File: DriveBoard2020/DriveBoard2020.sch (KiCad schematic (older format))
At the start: 66 parts, among them SW0 SW_SPST, SW1 SW_Push, SW3 SW_Push, SW5 SW_Push, SW7 SW_Push, SW8 SW_Push, SW9 SW_Push, U1 MAX_3232, U2 MAX_3232, U3 OKI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

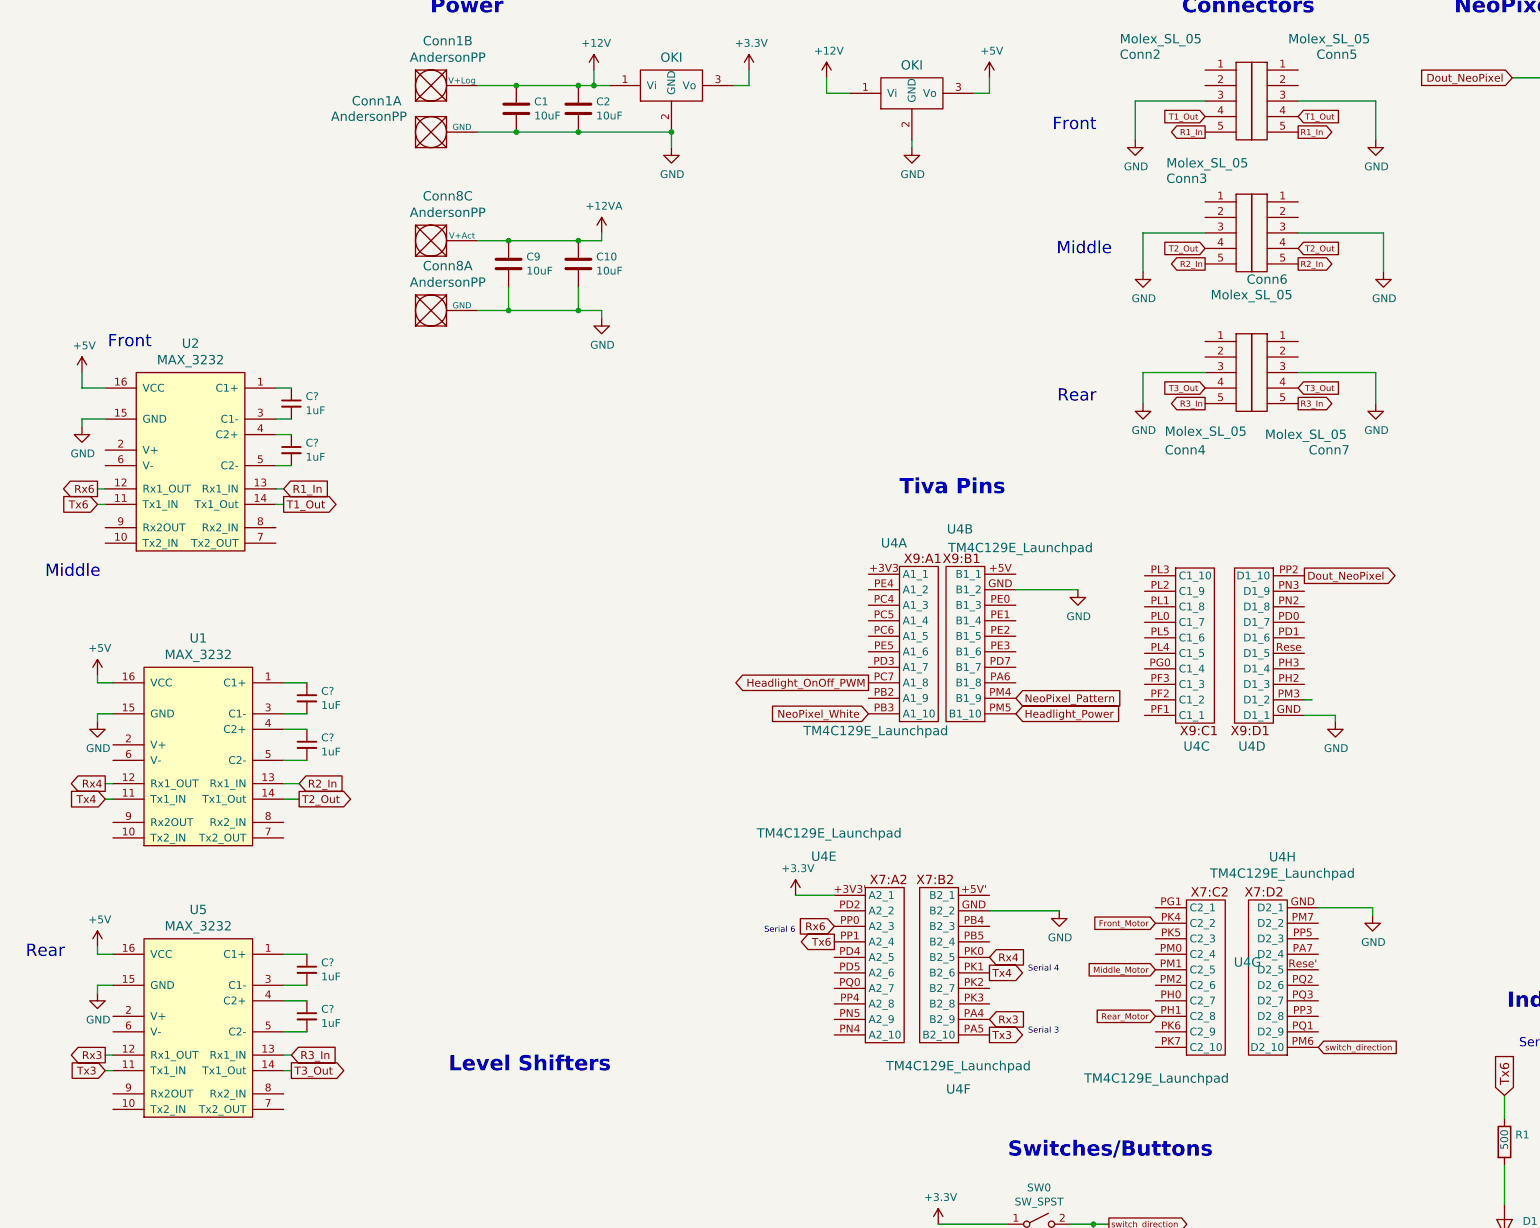
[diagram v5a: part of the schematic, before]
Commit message: added serials and relabled for individual wheel control
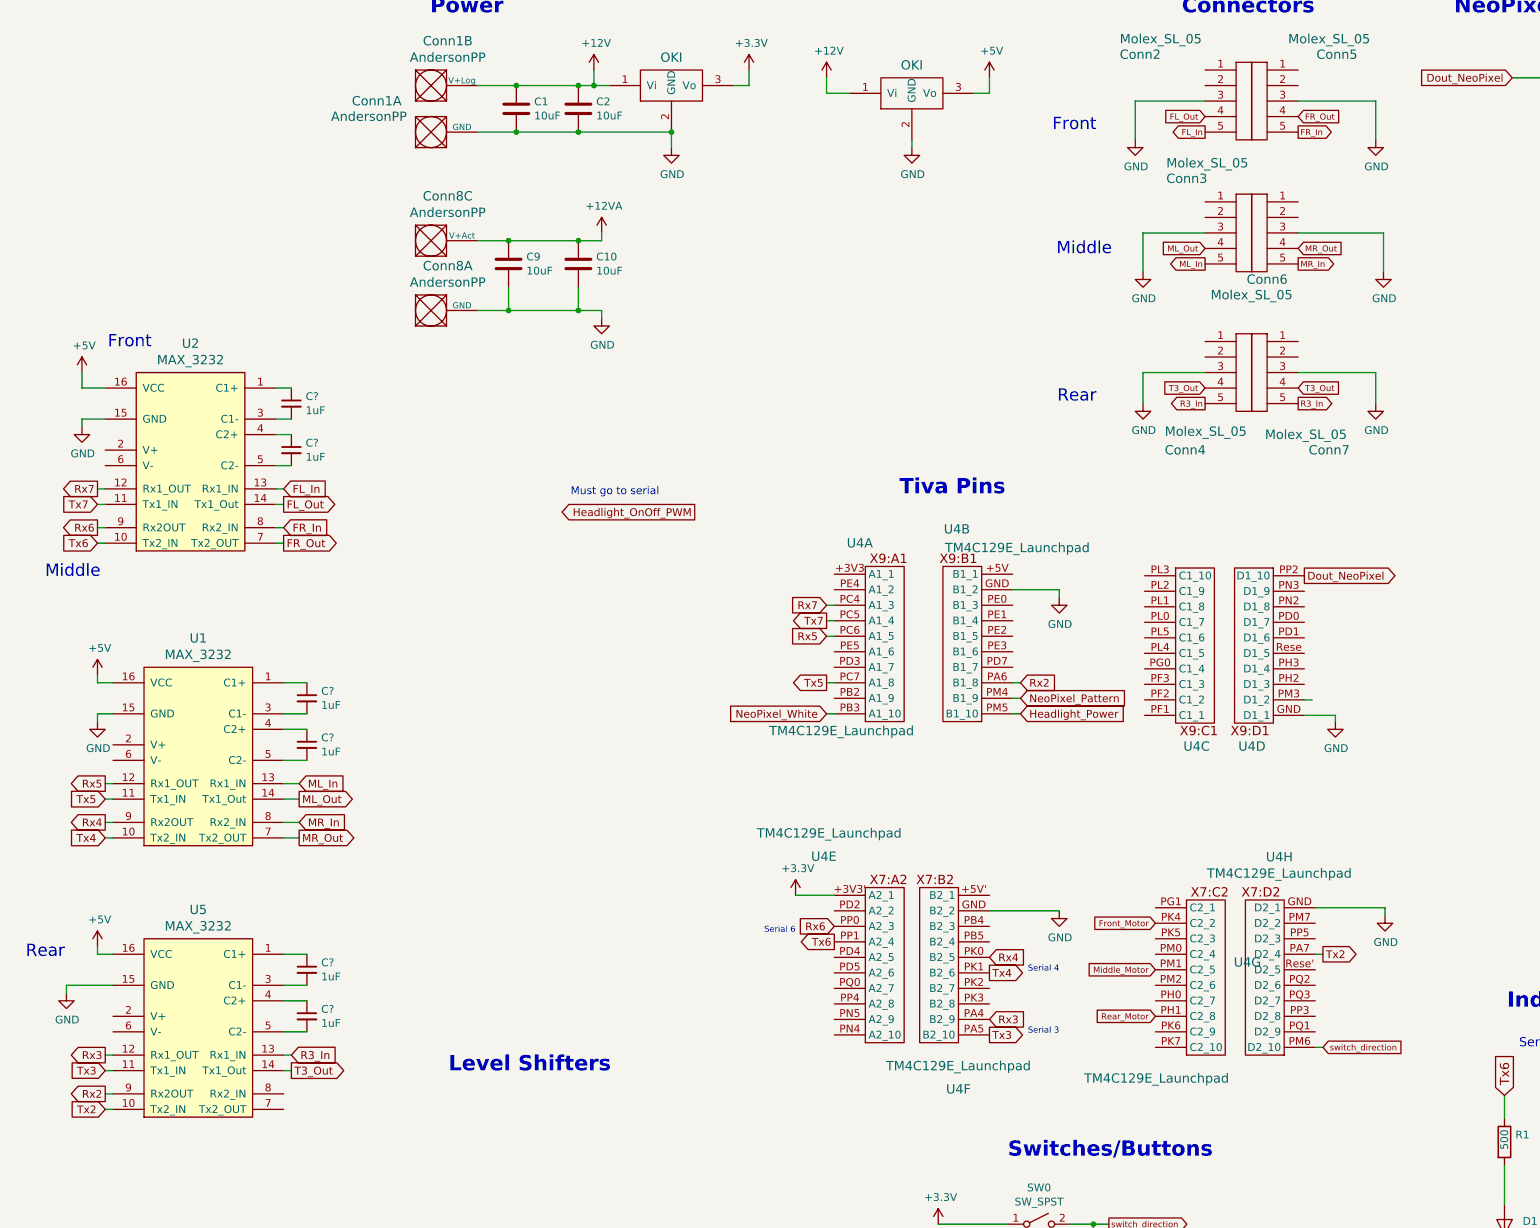
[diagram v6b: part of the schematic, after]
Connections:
- net Headlight_OnOff_PWM: no longer U4.PC7 (A1_8)
- net Rx4: now also U1.9 (Rx2OUT); no longer U1.12 (Rx1_OUT)
- net Rx6: now also U2.9 (Rx2OUT); no longer U2.12 (Rx1_OUT)
- net Tx4: now also U1.10 (Tx2_IN); no longer U1.11 (Tx1_IN)
- net Tx6: now also U2.10 (Tx2_IN); no longer U2.11 (Tx1_IN)
- net FR_Out: now reaches U2.7 (Tx2_OUT)
- net FR_Out: now also Conn5.4
- net FR_In: now reaches U2.8 (Rx2_IN)
- net FR_In: now also Conn5.5
- net Tx2: now reaches U5.10 (Tx2_IN)
- net Tx2: now also U4.PA7 (D2_4)
- net Rx2: now reaches U5.9 (Rx2OUT)
- net Rx2: now also U4.PA6 (B1_8)
- net MR_Out: now reaches U1.7 (Tx2_OUT)
- net MR_Out: now also Conn6.4
- net MR_In: now reaches U1.8 (Rx2_IN)
- net MR_In: now also Conn6.5
- net Rx7: now reaches U4.PC4 (A1_3)
- net Rx7: now also U2.12 (Rx1_OUT)
- net Tx7: now reaches U4.PC5 (A1_4)
- net Tx7: now also U2.11 (Tx1_IN)
- net Rx5: now reaches U4.PC6 (A1_5)
- net Rx5: now also U1.12 (Rx1_OUT)
- net R1_In renamed FL_In
- net FL_In: no longer Conn5.5
- net R2_In renamed ML_In
- net ML_In: no longer Conn6.5
- net T1_Out renamed FL_Out
- net FL_Out: no longer Conn5.4
- net T2_Out renamed ML_Out
- net ML_Out: no longer Conn6.4
- new net Tx5: U1.11 (Tx1_IN), U4.PC7 (A1_8)
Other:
- note added: "Must go to serial"
- moved on the sheet: U4A, U4B, U4H
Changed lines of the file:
@@
 Text GLabel 15300 2340 2    50   Output ~ 0
 NeoPixel_Pattern
-Text GLabel 9270 5250 2    50   Input ~ 0
+Text GLabel 9300 5250 2    50   Input ~ 0
 Headlight_Power
 Wire Wire Line
 	11180 5160 11130 5160
-Text GLabel 8320 5250 0    50   Input ~ 0
-NeoPixel_White
-Text GLabel 9270 5150 2    50   Input ~ 0
+Text GLabel 9300 5150 2    50   Input ~ 0
 NeoPixel_Pattern
 $Comp
@@
 	15020 4050 15020 4100
 Text GLabel 11090 1400 2    39   Input ~ 0
-T1_Out
+FR_Out
 $Comp
 L DriveBoard2020-rescue:Molex_SL_05-MRDT_Connectors-DriveBoard2020-rescue Conn5
@@
 $EndComp
 Text GLabel 11090 1500 2    39   Output ~ 0
-R1_In
+FR_In
 Wire Wire Line
 	3250 3350 3250 3400
@@
 Text GLabel 10170 6600 0    39   Input ~ 0
 Front_Motor
-Text GLabel 11220 7400 2    39   Input ~ 0
+Text GLabel 11250 7400 2    39   Input ~ 0
 switch_direction
 $Comp
@@
 $EndComp
 Text GLabel 10490 1400 0    39   Input ~ 0
-T1_Out
+FL_Out
 Text GLabel 10490 1500 0    39   Output ~ 0
-R1_In
+FL_In
 Text GLabel 10490 3150 0    39   Input ~ 0
 T3_Out
@@
 $EndComp
 Text GLabel 10490 2350 0    39   Output ~ 0
-R2_In
+ML_In
 Text GLabel 10490 2250 0    39   Input ~ 0
-T2_Out
+ML_Out
 $Comp
 L power:GND #PWR0114
@@
 Rear
 Text GLabel 11090 2250 2    39   Input ~ 0
-T2_Out
+MR_Out
 Text GLabel 11090 2350 2    39   Output ~ 0
-R2_In
+MR_In
 Text GLabel 11090 3150 2    39   Input ~ 0
 T3_Out
@@
 Text GLabel 3400 7550 0    50   Input ~ 0
 Tx3
-Text GLabel 4650 5700 2    50   Input ~ 0
-R2_In
-Text GLabel 4650 5800 2    50   Output ~ 0
-T2_Out
-Text GLabel 4550 3800 2    51   Input ~ 0
-R1_In
-Text GLabel 4550 3900 2    51   Output ~ 0
-T1_Out
-Text GLabel 3400 5700 0    50   Output ~ 0
+Text GLabel 4650 5950 2    50   Input ~ 0
+MR_In
+Text GLabel 4650 6050 2    50   Output ~ 0
+MR_Out
+Text GLabel 4550 4050 2    51   Input ~ 0
+FR_In
+Text GLabel 4550 4150 2    51   Output ~ 0
+FR_Out
+Text GLabel 3400 5950 0    50   Output ~ 0
 Rx4
-Text GLabel 3400 5800 0    51   Input ~ 0
+Text GLabel 3400 6050 0    51   Input ~ 0
 Tx4
-Text GLabel 3350 3800 0    50   Output ~ 0
+Text GLabel 3350 4050 0    50   Output ~ 0
 Rx6
-Text GLabel 3350 3900 0    51   Input ~ 0
+Text GLabel 3350 4150 0    51   Input ~ 0
 Tx6
 $Comp
@@
 $Comp
 L MRDT_Shields:TM4C129E_Launchpad U4
-U 1 1 5DE8D46B
-P 8520 5300
-F 0 "U4" H 8400 6450 60  0000 L CNN
-F 1 "TM4C129E_Launchpad" H 7900 5240 60  0000 L CNN
-F 2 "MRDT_Shields:TM4C129E_Launchpad_FULL_THT_BOTTOM" H 8520 5300 60  0001 C CNN
-F 3 "" H 8520 5300 60  0001 C CNN
-	1    8520 5300
-	1    0    0    -1
-$EndComp
-$Comp
-L MRDT_Shields:TM4C129E_Launchpad U4
 U 2 1 5DE90FB1
-P 9070 5300
-F 0 "U4" H 9230 6540 60  0000 C CNN
-F 1 "TM4C129E_Launchpad" H 8840 6420 60  0000 C CNN
-F 2 "MRDT_Shields:TM4C129E_Launchpad_FULL_THT_BOTTOM" H 9070 5300 60  0001 C CNN
-F 3 "" H 9070 5300 60  0001 C CNN
-	2    9070 5300
+P 9050 5300
+F 0 "U4" H 9210 6540 60  0000 C CNN
+F 1 "TM4C129E_Launchpad" H 8820 6420 60  0000 C CNN
+F 2 "MRDT_Shields:TM4C129E_Launchpad_FULL_THT_BOTTOM" H 9050 5300 60  0001 C CNN
+F 3 "" H 9050 5300 60  0001 C CNN
+	2    9050 5300
 	-1   0    0    -1
 $EndComp
@@
 L MRDT_Shields:TM4C129E_Launchpad U4
 U 8 1 5DEDFAF8
-P 11020 7450
-F 0 "U4" H 11051 8727 60  0000 C CNN
-F 1 "TM4C129E_Launchpad" H 11051 8621 60  0000 C CNN
-F 2 "MRDT_Shields:TM4C129E_Launchpad_FULL_THT_BOTTOM" H 11020 7450 60  0001 C CNN
-F 3 "" H 11020 7450 60  0001 C CNN
-	8    11020 7450
+P 11000 7450
+F 0 "U4" H 11031 8727 60  0000 C CNN
+F 1 "TM4C129E_Launchpad" H 11031 8621 60  0000 C CNN
+F 2 "MRDT_Shields:TM4C129E_Launchpad_FULL_THT_BOTTOM" H 11000 7450 60  0001 C CNN
+F 3 "" H 11000 7450 60  0001 C CNN
+	8    11000 7450
 	-1   0    0    -1
 $EndComp
-Text GLabel 8320 5050 0    50   Output ~ 0
-Headlight_OnOff_PWM
 Wire Wire Line
 	11330 5260 11330 5300
@@
 L power:GND #PWR0146
 U 1 1 5E44A8A8
-P 9670 4450
-F 0 "#PWR0146" H 9670 4200 50  0001 C CNN
-F 1 "GND" H 9675 4277 50  0000 C CNN
-F 2 "" H 9670 4450 50  0001 C CNN
-F 3 "" H 9670 4450 50  0001 C CNN
-	1    9670 4450
+P 9550 4500
+F 0 "#PWR0146" H 9550 4250 50  0001 C CNN
+F 1 "GND" H 9555 4327 50  0000 C CNN
+F 2 "" H 9550 4500 50  0001 C CNN
+F 3 "" H 9550 4500 50  0001 C CNN
+	1    9550 4500
 	1    0    0    -1
 $EndComp
@@
 L power:GND #PWR0150
 U 1 1 5E4D6DF7
-P 11570 6550
-F 0 "#PWR0150" H 11570 6300 50  0001 C CNN
-F 1 "GND" H 11575 6377 50  0000 C CNN
-F 2 "" H 11570 6550 50  0001 C CNN
-F 3 "" H 11570 6550 50  0001 C CNN
-	1    11570 6550
+P 11650 6550
+F 0 "#PWR0150" H 11650 6300 50  0001 C CNN
+F 1 "GND" H 11655 6377 50  0000 C CNN
+F 2 "" H 11650 6550 50  0001 C CNN
+F 3 "" H 11650 6550 50  0001 C CNN
+	1    11650 6550
 	1    0    0    -1
 $EndComp
@@
 	1    0    0    -1
 $EndComp
-Wire Wire Line
-	9270 4450 9670 4450
 $Comp
 L power:+5V #PWR0154
@@
 	1    0    0    -1
 $EndComp
-Wire Wire Line
-	11220 6500 11570 6500
-Wire Wire Line
-	11570 6500 11570 6550
 Wire Notes Line
 	11790 9960 11810 9960
@@
 L power:GND #PWR?
 U 1 1 5E239C6D
-P 3350 7050
-F 0 "#PWR?" H 3350 6800 50  0001 C CNN
-F 1 "GND" H 3355 6877 50  0000 C CNN
-F 2 "" H 3350 7050 50  0001 C CNN
-F 3 "" H 3350 7050 50  0001 C CNN
-	1    3350 7050
-	1    0    0    -1
-$EndComp
-Wire Wire Line
-	3450 7000 3350 7000
-Wire Wire Line
-	3350 7000 3350 7050
+P 3150 7050
+F 0 "#PWR?" H 3150 6800 50  0001 C CNN
+F 1 "GND" H 3155 6877 50  0000 C CNN
+F 2 "" H 3150 7050 50  0001 C CNN
+F 3 "" H 3150 7050 50  0001 C CNN
+	1    3150 7050
+	1    0    0    -1
+$EndComp
 $Comp
 L Device:C_Small C?
@@
 	1    0    0    -1
 $EndComp
+$Comp
+L MRDT_Shields:TM4C129E_Launchpad U4
+U 1 1 5DE8D46B
+P 8300 5300
+F 0 "U4" H 8180 6450 60  0000 L CNN
+F 1 "TM4C129E_Launchpad" H 7680 5240 60  0000 L CNN
+F 2 "MRDT_Shields:TM4C129E_Launchpad_FULL_THT_BOTTOM" H 8300 5300 60  0001 C CNN
+F 3 "" H 8300 5300 60  0001 C CNN
+	1    8300 5300
+	1    0    0    -1
+$EndComp
+Text GLabel 8050 5250 0    50   Input ~ 0
+NeoPixel_White
+Text GLabel 7200 3950 0    50   Output ~ 0
+Headlight_OnOff_PWM
+Wire Wire Line
+	8050 5050 8100 5050
+Wire Wire Line
+	8050 5250 8100 5250
+Wire Wire Line
+	8100 4550 8050 4550
+Wire Wire Line
+	8100 4650 8050 4650
+Text GLabel 8050 4550 0    50   Input ~ 0
+Rx7
+Text GLabel 8050 4650 0    50   Output ~ 0
+Tx7
+Wire Wire Line
+	8100 4750 8050 4750
+Text Notes 6400 3850 0    50   ~ 0
+Must go to serial
+Text GLabel 8050 4750 0    50   Input ~ 0
+Rx5
+Text GLabel 8050 5050 0    50   Output ~ 0
+Tx5
+Wire Wire Line
+	9250 4450 9550 4450
+Wire Wire Line
+	9550 4450 9550 4500
+Wire Wire Line
+	9250 5050 9300 5050
+Wire Wire Line
+	9250 5150 9300 5150
+Wire Wire Line
+	9250 5250 9300 5250
+Text GLabel 9300 5050 2    50   Input ~ 0
+Rx2
+Wire Wire Line
+	11200 7400 11250 7400
+Wire Wire Line
+	11650 6500 11650 6550
+Wire Wire Line
+	11200 6500 11650 6500
+Wire Wire Line
+	11200 6800 11250 6800
+Text GLabel 11250 6800 2    50   Output ~ 0
+Tx2
+Text GLabel 3400 7700 0    50   Output ~ 0
+Rx2
+Text GLabel 3400 7800 0    50   Input ~ 0
+Tx2
+Wire Wire Line
+	3400 7700 3450 7700
+Wire Wire Line
+	3400 7800 3450 7800
+Wire Wire Line
+	3450 5950 3400 5950
+Wire Wire Line
+	3450 6050 3400 6050
+Wire Wire Line
+	4550 5950 4650 5950
+Wire Wire Line
+	4550 6050 4650 6050
+Text GLabel 3400 5700 0    50   Output ~ 0
+Rx5
+Text GLabel 3400 5800 0    51   Input ~ 0
+Tx5
+Wire Wire Line
+	3400 4050 3350 4050
+Wire Wire Line
+	3400 4150 3350 4150
+Wire Wire Line
+	4500 4050 4550 4050
+Wire Wire Line
+	4500 4150 4550 4150
+Text GLabel 3350 3800 0    50   Output ~ 0
+Rx7
+Text GLabel 3350 3900 0    51   Input ~ 0
+Tx7
+Text GLabel 4550 3800 2    51   Input ~ 0
+FL_In
+Text GLabel 4550 3900 2    51   Output ~ 0
+FL_Out
+Text GLabel 4650 5700 2    50   Input ~ 0
+ML_In
+Text GLabel 4650 5800 2    50   Output ~ 0
+ML_Out
+Wire Wire Line
+	3150 7050 3150 7000
+Wire Wire Line
+	3150 7000 3450 7000
 $EndSCHEMATC
